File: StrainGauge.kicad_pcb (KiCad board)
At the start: 2 copper layers, 29 x 41 mm, 33 parts, among them J1 Conn_01x04, J2 502585-0470, U1 INA333xxDGK, U2 REF2025, U3 OPA310xDBV, U4 OPA310xDBV

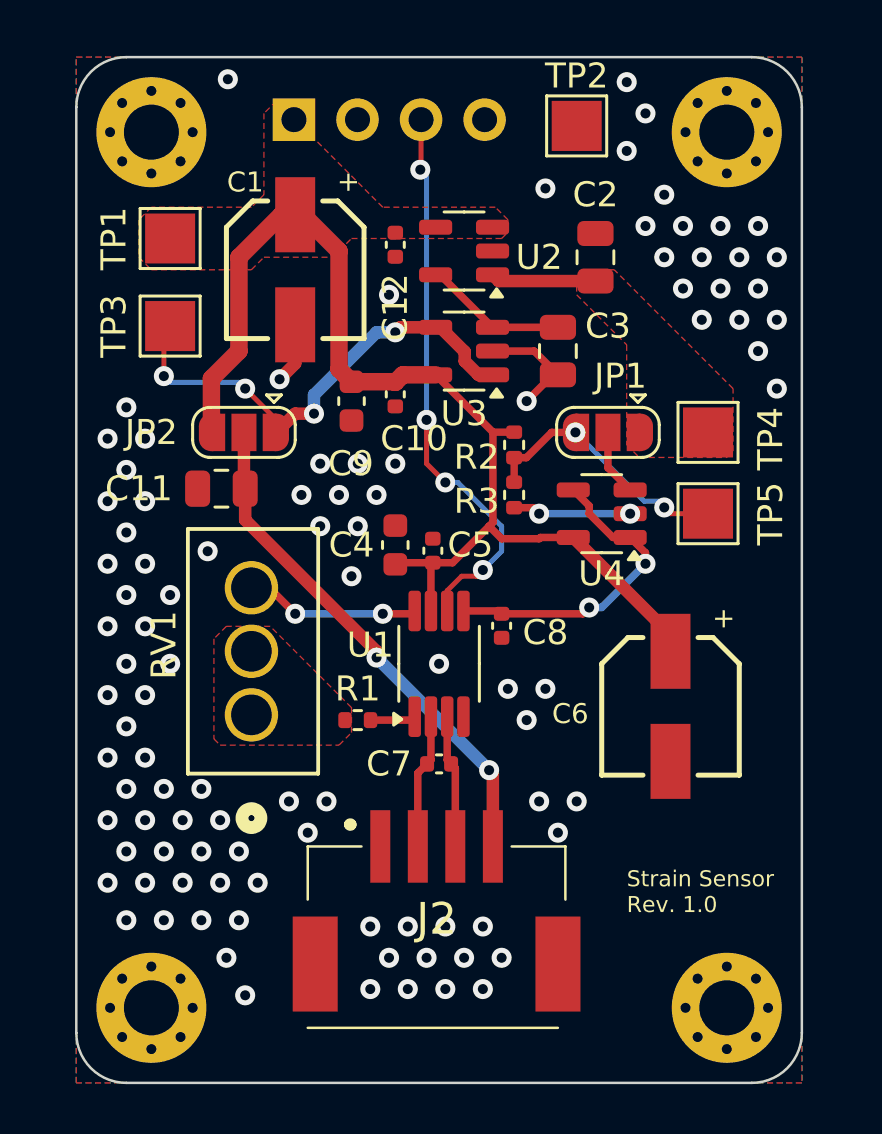
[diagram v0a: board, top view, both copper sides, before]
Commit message: fixed constraint violations
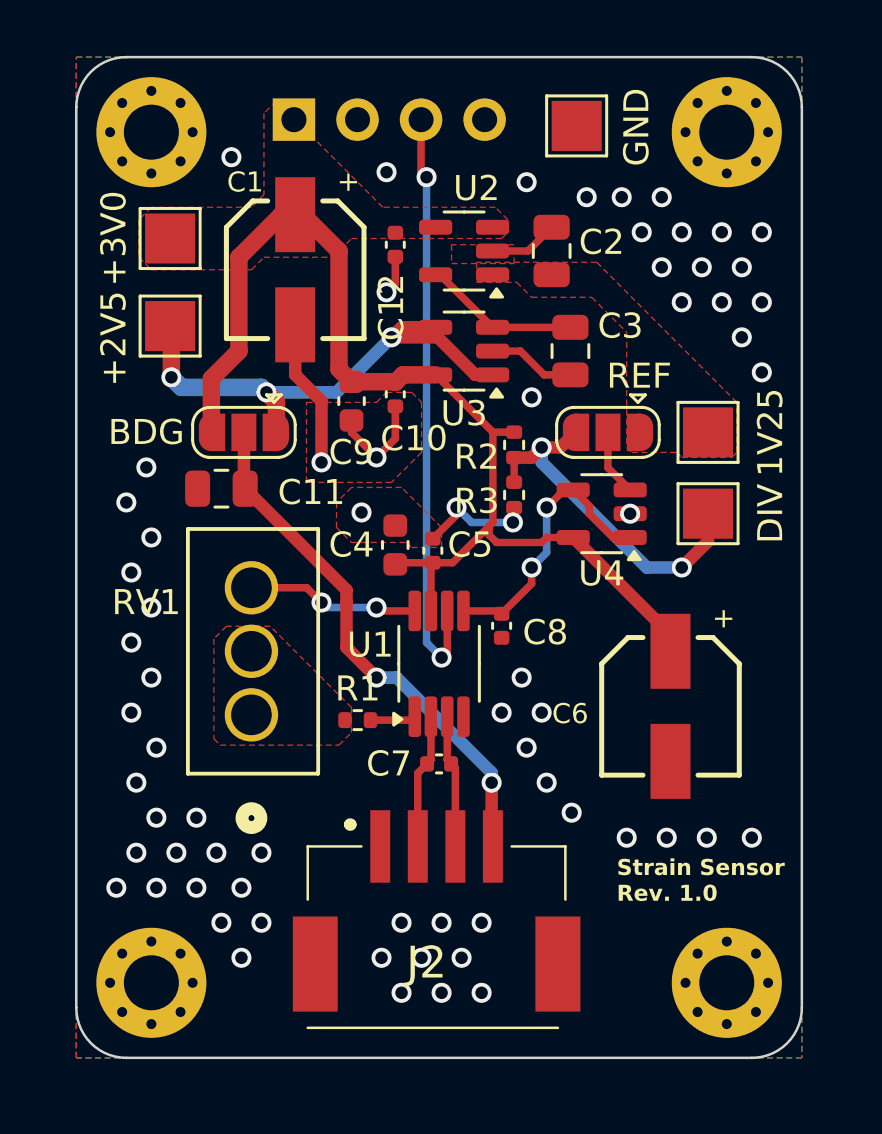
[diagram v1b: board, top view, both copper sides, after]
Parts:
- moved C2 1.77 mm to (148.0, 99.8)
- moved H3 1.00 mm to (155.0, 129.0)
- moved H4 1.00 mm to (132.0, 129.0)
- moved C3 0.50 mm to (148.8, 103.8)
- renumbered TP3 to +2V5, TP1 to +3V0, TP4 to 1V25, JP2 to BDG, TP5 to DIV, TP2 to GND, JP1 to REF
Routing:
- net GND: track 11.9 -> 22.8 mm, vias 101 -> 68
- net /Vbias: track 4.22 -> 0.00 mm
- net /AmpOffset: track 10.5 -> 14.4 mm
- net /AmpRef: track 12.7 -> 11.2 mm
- net /ADC: track 22.5 -> 23.8 mm, vias 4 -> 2
- net +2V5: track 19.7 -> 20.4 mm, vias 4 -> 3
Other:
- board size 29 x 41 mm -> 29 x 40 mm

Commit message: added gerbers
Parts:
- removed +2V5, +3V0, 1V25, DIV, GND: TestPoint, TestPoint:TestPoint_Pad_2.0x2.0mm
- removed BDG, REF: SolderJumper_3_Open, Jumper:SolderJumper-3_P1.3mm_Open_RoundedPad1.0x1.5mm
- added JP1: SolderJumper_3_Open, Jumper:SolderJumper-3_P1.3mm_Open_RoundedPad1.0x1.5mm, F.Cu at (150.2, 106.8)
- added JP2: SolderJumper_3_Open, Jumper:SolderJumper-3_P1.3mm_Open_RoundedPad1.0x1.5mm, F.Cu at (135.7, 107.0)
- added JP3: SolderJumper_2_Open, Jumper:SolderJumper-2_P1.3mm_Open_RoundedPad1.0x1.5mm, F.Cu at (149.2, 94.6)
- added TP1: TestPoint, TestPoint:TestPoint_Pad_2.0x2.0mm, F.Cu at (132.8, 99.2)
- added TP2: TestPoint, TestPoint:TestPoint_Pad_2.0x2.0mm, F.Cu at (131.4, 116.8)
- added TP3: TestPoint, TestPoint:TestPoint_Pad_2.0x2.0mm, F.Cu at (132.8, 102.8)
- added TP4: TestPoint, TestPoint:TestPoint_Pad_2.0x2.0mm, F.Cu at (154.2, 106.8)
- added TP5: TestPoint, TestPoint:TestPoint_Pad_2.0x2.0mm, F.Cu at (154.2, 110.2)
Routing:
- net /AmpRef: track 11.2 -> 26.4 mm, vias 2 -> 4
- net /AREF: track 0.00 -> 9.59 mm
- net /Vbdg+: track 21.1 -> 22.3 mm
- net GND: track 22.8 -> 23.8 mm, vias 68 -> 71
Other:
- board text added: "+1V25"
- board text added: "+2V5"
- board text added: "+3V0"
- board text added: "ADC"
- board text added: "AREF"
- board text added: "BDG"
- board text added: "DIV"
- board text added: "GND"
- board text added: "REF"
- board text added: "Wireless Sensors Project: Full-Bridge Strain Gauge Sensor Ilyas Asmouki, Alexandros Dellios, Noé Siméon Dumez, Rosana Balasingam"

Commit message: small fixes
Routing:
- net GND: vias 71 -> 83
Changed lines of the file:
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@@
 			(drillshape 0)
 			(scaleselection 1)
-			(outputdirectory "Gerbers/")
+			(outputdirectory "PDFs/")
 		)
 	)
@@
 		(tags "test point SMD pad rectangle square")
 		(property "Reference" "TP2"
-			(at 0 -1.998 360)
+			(at 0 -1.998 0)
 			(layer "F.SilkS")
 			(hide yes)
@@
 		)
 		(property "Value" "TestPoint"
-			(at 0 2.05 360)
+			(at 0 2.05 0)
 			(layer "F.Fab")
 			(effects
@@
 		)
 		(fp_text user "${REFERENCE}"
-			(at 0 -2.000001 360)
+			(at 0 -2.000001 0)
 			(layer "F.Fab")
 			(effects
@@
 		(tags "solder jumper open")
 		(property "Reference" "JP1"
-			(at -1.2 2.2 360)
+			(at -1.2 2.2 0)
 			(layer "F.SilkS")
 			(hide yes)
@@
 		)
 		(property "Value" "SolderJumper_3_Open"
-			(at 0 1.9 360)
+			(at 0 1.9 0)
 			(layer "F.Fab")
 			(effects
@@
 		(tags "solder jumper open")
 		(property "Reference" "JP2"
-			(at 3.7 0.2 360)
+			(at 3.7 0.2 0)
 			(layer "F.SilkS")
 			(hide yes)
@@
 		)
 		(property "Value" "SolderJumper_3_Open"
-			(at 0 1.9 360)
+			(at 0 1.9 0)
 			(layer "F.Fab")
 			(effects
@@
 	)
 	(via
+		(at 139.6 123.8)
+		(size 0.8)
+		(drill 0.5)
+		(layers "F.Cu" "B.Cu")
+		(free yes)
+		(net 2)
+	)
+	(via
 		(at 132 111.2)
 		(size 0.8)
@@
 	)
 	(via
+		(at 148.8 124.8)
+		(size 0.8)
+		(drill 0.5)
+		(layers "F.Cu" "B.Cu")
+		(free yes)
+		(net 2)
+	)
+	(via
+		(at 156.6 118)
+		(size 0.8)
+		(drill 0.5)
+		(layers "F.Cu" "B.Cu")
+		(free yes)
+		(net 2)
+	)
+	(via
 		(at 135.6 128)
 		(size 0.8)
@@
 	)
 	(via
+		(at 131 105.4)
+		(size 0.8)
+		(drill 0.5)
+		(layers "F.Cu" "B.Cu")
+		(free yes)
+		(net 2)
+	)
+	(via
 		(at 146.452498 110.6)
 		(size 0.8)
@@
 	)
 	(via
+		(at 147.6 96.8)
+		(size 0.8)
+		(drill 0.5)
+		(layers "F.Cu" "B.Cu")
+		(free yes)
+		(net 2)
+	)
+	(via
 		(at 145.2 129.4)
 		(size 0.8)
@@
 	)
 	(via
+		(at 149.6 115)
+		(size 0.8)
+		(drill 0.5)
+		(layers "F.Cu" "B.Cu")
+		(free yes)
+		(net 2)
+	)
+	(via
 		(at 133.8 125.2)
 		(size 0.8)
@@
 	)
 	(via
+		(at 147.8 123.4)
+		(size 0.8)
+		(drill 0.5)
+		(layers "F.Cu" "B.Cu")
+		(free yes)
+		(net 2)
+	)
+	(via
 		(at 154.2 123.2)
 		(size 0.8)
@@
 	)
 	(via
+		(at 156.6 114.4)
+		(size 0.8)
+		(drill 0.5)
+		(layers "F.Cu" "B.Cu")
+		(free yes)
+		(net 2)
+	)
+	(via
 		(at 132.2 125.2)
 		(size 0.8)
@@
 	)
 	(via
+		(at 155.2 121.8)
+		(size 0.8)
+		(drill 0.5)
+		(layers "F.Cu" "B.Cu")
+		(free yes)
+		(net 2)
+	)
+	(via
 		(at 130.6 122.4)
 		(size 0.8)
@@
 	)
 	(via
+		(at 156.6 116.2)
+		(size 0.8)
+		(drill 0.5)
+		(layers "F.Cu" "B.Cu")
+		(free yes)
+		(net 2)
+	)
+	(via
 		(at 142 126.6)
 		(size 0.8)
@@
 	)
 	(via
+		(at 156.6 112.6)
+		(size 0.8)
+		(drill 0.5)
+		(layers "F.Cu" "B.Cu")
+		(free yes)
+		(net 2)
+	)
+	(via
+		(at 156.6 120)
+		(size 0.8)
+		(drill 0.5)
+		(layers "F.Cu" "B.Cu")
+		(free yes)
+		(net 2)
+	)
+	(via
 		(at 131.4 123.8)
 		(size 0.8)
@@
 		(hatch edge 0.5)
 		(connect_pads
-			(clearance 0.5)
+			(clearance 0.15)
 		)
-		(min_thickness 0.25)
+		(min_thickness 0.15)
 		(filled_areas_thickness no)
 		(fill yes

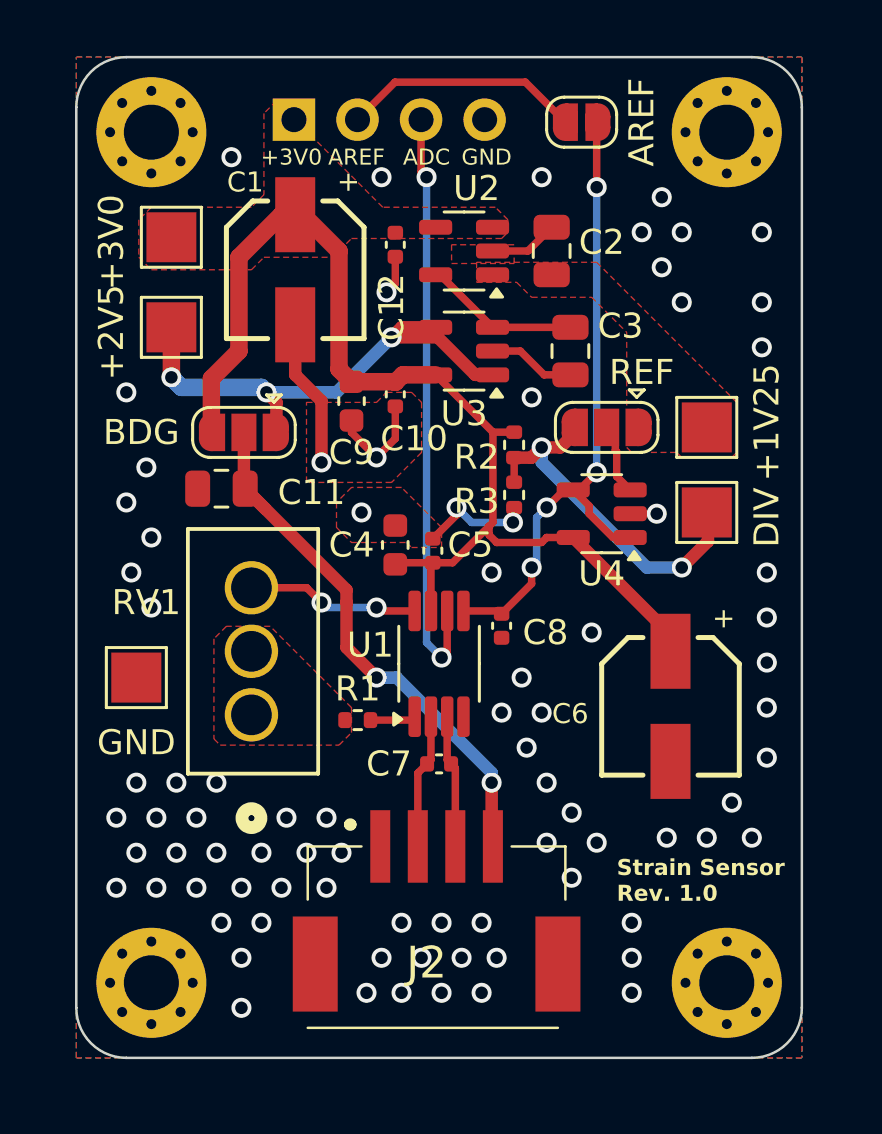
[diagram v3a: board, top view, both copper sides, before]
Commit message: added power connector for external battery
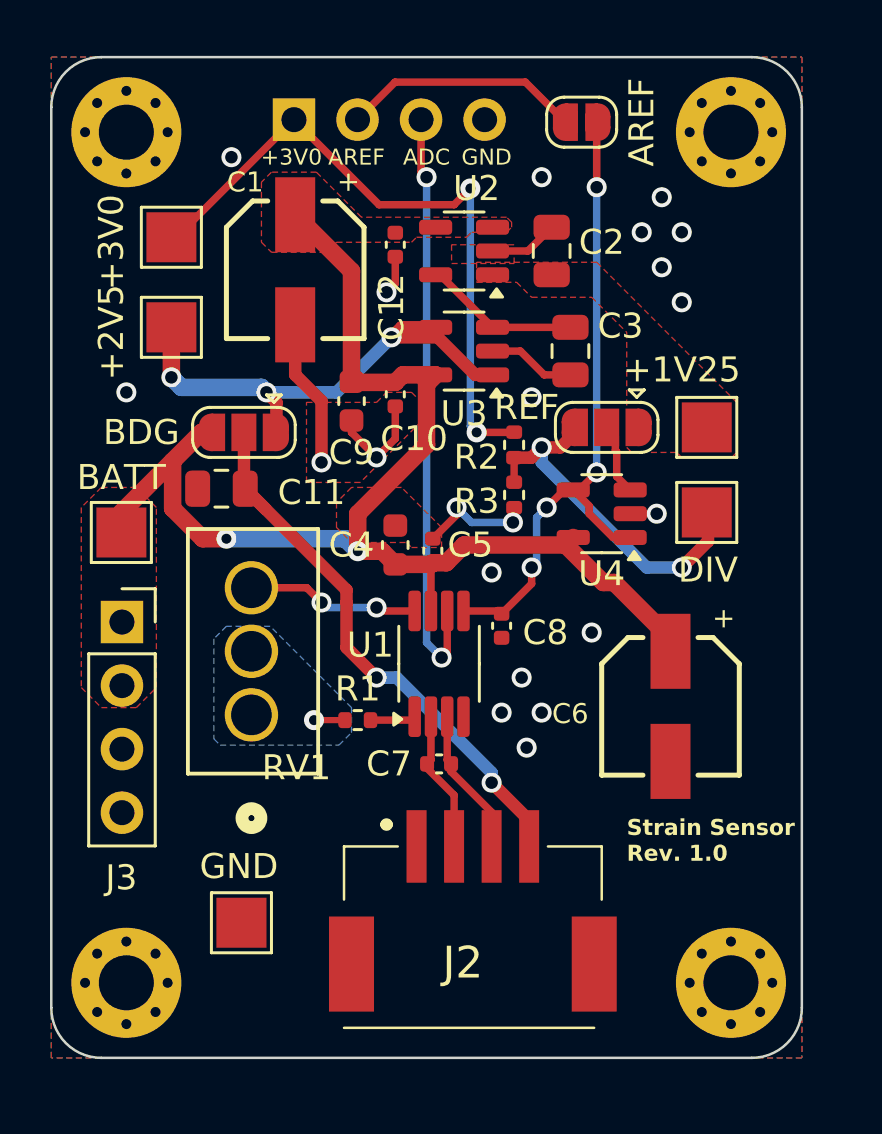
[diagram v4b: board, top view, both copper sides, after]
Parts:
- added J3: Conn_01x04, Connector_PinSocket_2.54mm:PinSocket_1x04_P2.54mm_Vertical, F.Cu at (130.8, 114.6)
- added TP6: TestPoint, TestPoint:TestPoint_Pad_2.0x2.0mm, F.Cu at (130.8, 111.0)
- moved TP2 10.7 mm to (135.6, 126.6)
- moved J2 1.45 mm to (144.8, 127.2)
- moved H1 1.00 mm to (131.0, 95.0)
- moved H4 1.00 mm to (131.0, 129.0)
- moved H2 0.17 mm to (155.2, 95.0)
- moved H3 0.17 mm to (155.2, 129.0)
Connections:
- C1 pad 1: VCC -> +BATT
- C10 pad 1: VCC -> +BATT
- C12 pad 1: VCC -> +BATT
- C4 pad 1: VCC -> +BATT
- C5 pad 1: VCC -> +BATT
- C6 pad 1: VCC -> +BATT
- C9 pad 1: VCC -> +BATT
- JP2 pad 3: VCC -> +BATT
- U1 pad 7: VCC -> +BATT
- U2 pad 3: VCC -> +BATT
- U2 pad 4: VCC -> +BATT
- U3 pad 5: VCC -> +BATT
- U4 pad 5: VCC -> +BATT
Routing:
- net +BATT: track 0.00 -> 52.6 mm, vias 0 -> 2
- net VCC: track 46.0 -> 26.9 mm, vias 0 -> 2
- net /Rseries: track 0.30 -> 1.54 mm, vias 0 -> 1
- net /Vout+: track 5.32 -> 5.99 mm
- net /Vbdg+: track 22.3 -> 22.9 mm
- net GND: vias 83 -> 21
- added copper zone on F.Cu, net +BATT
- added copper zone on B.Cu, net /Rseries
- removed copper zone on F.Cu, net /Rseries
- removed copper zone on F.Cu, net VCC
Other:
- board size 29 x 40 mm -> 30 x 40 mm
- board text added: "BATT"

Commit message: added production files
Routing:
- net +BATT: track 52.6 -> 53.6 mm
- net GND: track 23.8 -> 23.0 mm, vias 21 -> 20
- net /Vbdg+: track 22.9 -> 23.5 mm
